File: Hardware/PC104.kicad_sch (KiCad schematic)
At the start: 44 parts, among them J10 J-0532610871, J11 J-TSW-106-05-T-S, J12 J-0532610671, J13 J-0532610471, J14 J-0532610471, J15 J-TSW-106-05-T-S, J16 J-0532610671, J17 J-0532610471, J2 2-Pin Header, J3 ESQ-126-14-G-D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

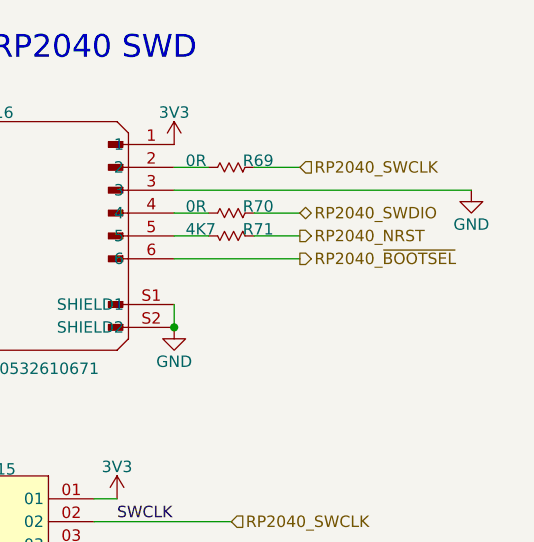
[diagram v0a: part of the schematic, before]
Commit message: Fix RP2040 BOOTSEL
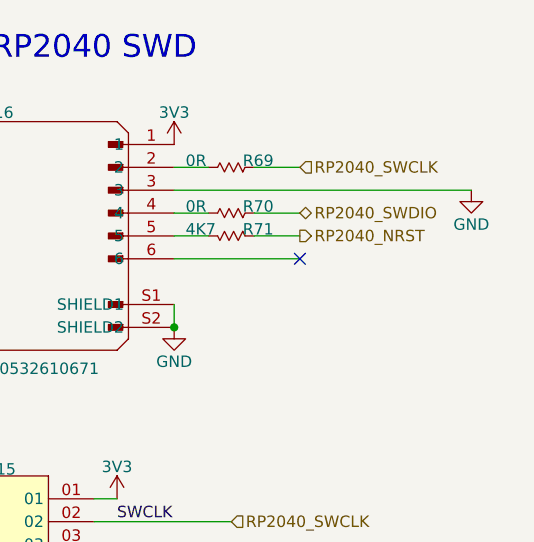
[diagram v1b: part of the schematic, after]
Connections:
- net RP2040_~{BOOTSEL}: no longer J16.6
- no-connect marks 2 -> 3
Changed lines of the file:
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@@
+	)
+	(no_connect
+		(at 356.87 49.53)
 	)
 	(no_connect
@@
 		)
 	)
-	(hierarchical_label "RP2040_~{BOOTSEL}"
-		(shape output)
-		(at 356.87 49.53 0)
-		(effects
-			(font
-				(size 1.27 1.27)
-			)
-			(justify left)
-		)
-	)

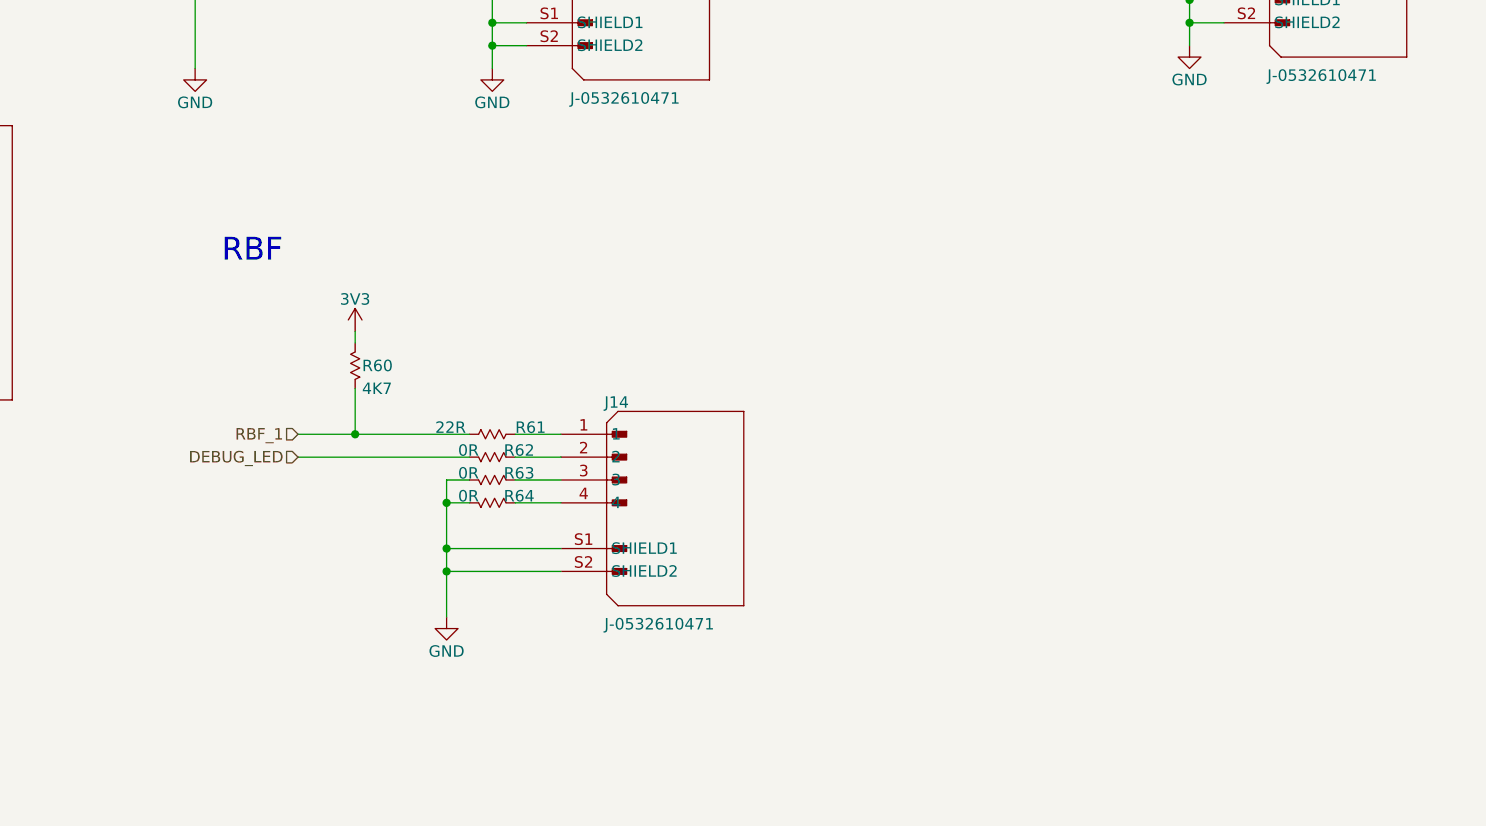
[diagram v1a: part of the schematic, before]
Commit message: Add IOC and second burnwire connector
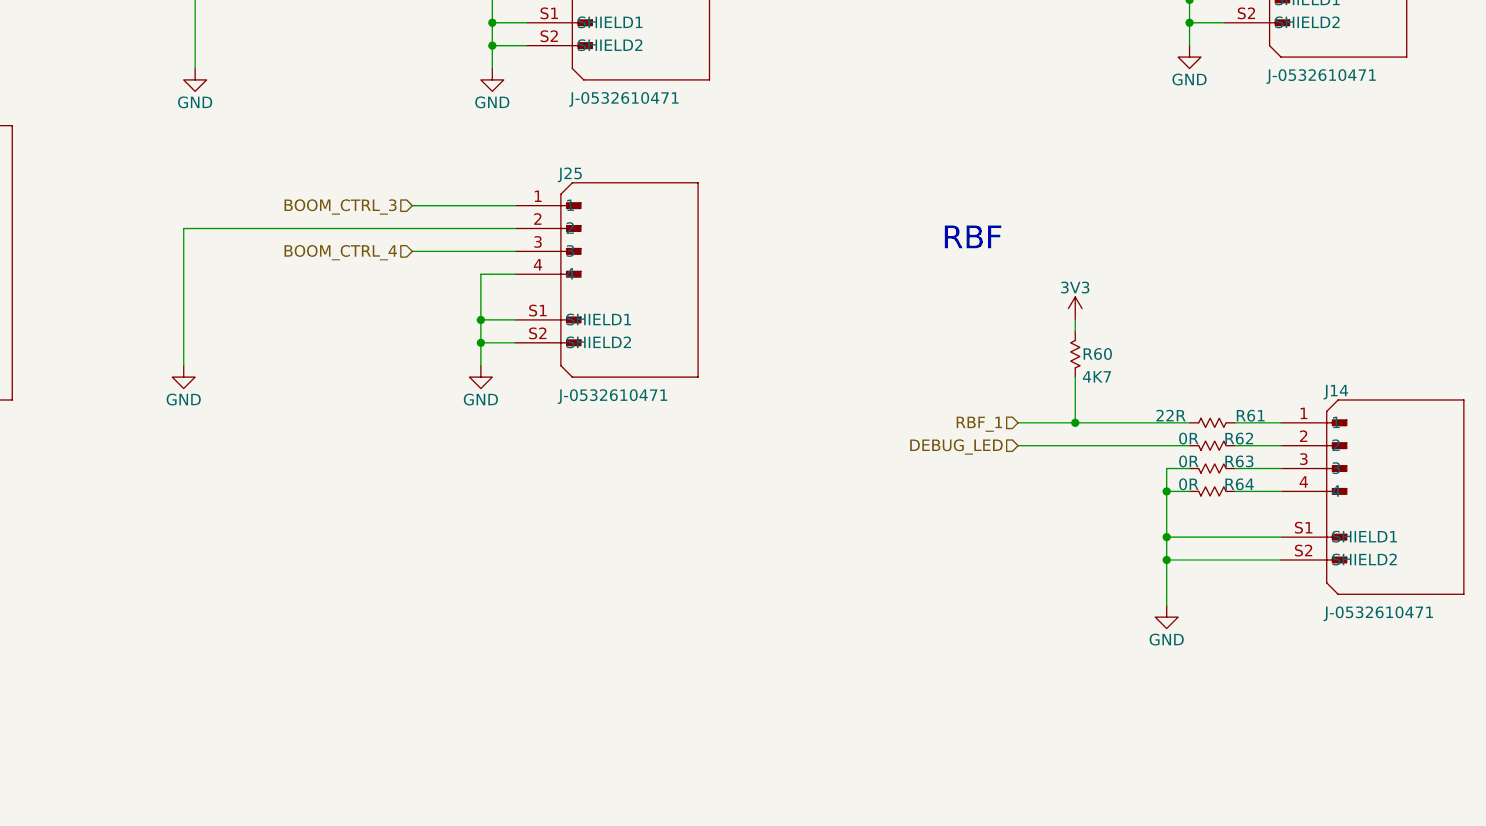
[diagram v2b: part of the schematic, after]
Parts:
- added J25: J-0532610471, J-53261-0471, symbol OBC Development Board:root_0_J-0532610471_OBC Development Board.SchLib
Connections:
- net GND: now also J25.2, J25.4, J25.S1 (SHIELD1), J25.S2 (SHIELD2)
- new net BOOM_CTRL_3: J25.1
- new net BOOM_CTRL_4: J25.3
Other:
- moved on the sheet: J14, R60, R61, R62, R63, R64

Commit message: Assign footprints
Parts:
- C36, C37, C38: footprint (none) -> Capacitor_SMD:C_1206_3216Metric
- D4, D5, D6: footprint (none) -> CTS-SAT-1:D-SML-D12U1WT86
- J10, J9: footprint J-532610871 -> CTS-SAT-1:J-532610871
- J11, J15: footprint J-TSW-106-05-T-S -> CTS-SAT-1:J-TSW-106-05-T-S
- J12, J16, J7: footprint J-0532610671 -> CTS-SAT-1:J-0532610671
- J13, J14, J17, J25, J8: footprint J-53261-0471 -> CTS-SAT-1:J-53261-0471
- J2, J5, J6: footprint (none) -> Connector_PinHeader_1.27mm:PinHeader_1x02_P1.27mm_Vertical
- R50, R51, R52, R53, R54: footprint (none) -> Resistor_SMD:R_0603_1608Metric
- R55, R56, R57, R58, R59, R60, R61, R62, R63, R64, R65, R66, R67, R68, R69, R70, R71: footprint 0603 -> Resistor_SMD:R_0603_1608Metric
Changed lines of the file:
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@@
 			)
 		)
-		(property "Footprint" "0603"
+		(property "Footprint" "Resistor_SMD:R_0603_1608Metric"
 			(at 354.33 187.96 0)
 			(effects
@@
 			)
 		)
-		(property "Footprint" "0603"
+		(property "Footprint" "Resistor_SMD:R_0603_1608Metric"
 			(at 354.33 185.42 0)
 			(effects
@@
 			)
 		)
-		(property "Footprint" "0603"
+		(property "Footprint" "Resistor_SMD:R_0603_1608Metric"
 			(at 285.75 49.53 0)
 			(effects
@@
 			)
 		)
-		(property "Footprint" "J-0532610671"
+		(property "Footprint" "CTS-SAT-1:J-0532610671"
 			(at 264.16 46.99 0)
 			(effects
@@
 			)
 		)
-		(property "Footprint" "J-TSW-106-05-T-S"
+		(property "Footprint" "CTS-SAT-1:J-TSW-106-05-T-S"
 			(at 321.31 83.82 0)
 			(effects
@@
 			)
 		)
-		(property "Footprint" "0603"
+		(property "Footprint" "Resistor_SMD:R_0603_1608Metric"
 			(at 285.75 46.99 0)
 			(effects
@@
 			)
 		)
-		(property "Footprint" "J-53261-0471"
+		(property "Footprint" "CTS-SAT-1:J-53261-0471"
 			(at 377.19 195.58 0)
 			(effects
@@
 			)
 		)
-		(property "Footprint" "0603"
+		(property "Footprint" "Resistor_SMD:R_0603_1608Metric"
 			(at 193.04 157.48 0)
 			(effects
@@
 			)
 		)
-		(property "Footprint" ""
+		(property "Footprint" "Capacitor_SMD:C_1206_3216Metric"
 			(at 108.9152 43.18 0)
 			(effects
@@
 			)
 		)
-		(property "Footprint" ""
+		(property "Footprint" "Resistor_SMD:R_0603_1608Metric"
 			(at 90.424 225.044 90)
 			(effects
@@
 			)
 		)
-		(property "Footprint" "0603"
+		(property "Footprint" "Resistor_SMD:R_0603_1608Metric"
 			(at 351.79 46.99 0)
 			(effects
@@
 			)
 		)
-		(property "Footprint" "J-TSW-106-05-T-S"
+		(property "Footprint" "CTS-SAT-1:J-TSW-106-05-T-S"
 			(at 256.54 83.82 0)
 			(effects
@@
 			)
 		)
-		(property "Footprint" ""
+		(property "Footprint" "CTS-SAT-1:D-SML-D12U1WT86"
 			(at 105.41 241.3 0)
 			(effects
@@
 			)
 		)
-		(property "Footprint" ""
+		(property "Footprint" "Connector_PinHeader_1.27mm:PinHeader_1x02_P1.27mm_Vertical"
 			(at 54.61 167.64 0)
 			(effects
@@
 			)
 		)
-		(property "Footprint" "0603"
+		(property "Footprint" "Resistor_SMD:R_0603_1608Metric"
 			(at 285.75 44.45 0)
 			(effects
@@
 			)
 		)
-		(property "Footprint" "0603"
+		(property "Footprint" "Resistor_SMD:R_0603_1608Metric"
 			(at 351.79 44.45 0)
 			(effects
@@
 			)
 		)
-		(property "Footprint" ""
+		(property "Footprint" "Resistor_SMD:R_0603_1608Metric"
 			(at 90.424 240.284 90)
 			(effects
@@
 			)
 		)
-		(property "Footprint" "J-53261-0471"
+		(property "Footprint" "CTS-SAT-1:J-53261-0471"
 			(at 293.37 138.43 0)
 			(effects
@@
 			)
 		)
-		(property "Footprint" "0603"
+		(property "Footprint" "Resistor_SMD:R_0603_1608Metric"
 			(at 351.79 39.37 0)
 			(effects
@@
 			)
 		)
-		(property "Footprint" ""
+		(property "Footprint" "CTS-SAT-1:D-SML-D12U1WT86"
 			(at 105.41 226.06 0)
 			(effects
@@
 			)
 		)
-		(property "Footprint" ""
+		(property "Footprint" "CTS-SAT-1:D-SML-D12U1WT86"
 			(at 105.41 233.68 0)
 			(effects
@@
 			)
 		)
-		(property "Footprint" ""
+		(property "Footprint" "Resistor_SMD:R_0603_1608Metric"
 			(at 90.424 232.664 90)
 			(effects
@@
 			)
 		)
-		(property "Footprint" "0603"
+		(property "Footprint" "Resistor_SMD:R_0603_1608Metric"
 			(at 354.33 182.88 0)
 			(effects
@@
 			)
 		)
-		(property "Footprint" "0603"
+		(property "Footprint" "Resistor_SMD:R_0603_1608Metric"
 			(at 198.12 167.64 0)
 			(effects
@@
 			)
 		)
-		(property "Footprint" "0603"
+		(property "Footprint" "Resistor_SMD:R_0603_1608Metric"
 			(at 193.04 160.02 0)
 			(effects
@@
 			)
 		)
-		(property "Footprint" ""
+		(property "Footprint" "Connector_PinHeader_1.27mm:PinHeader_1x02_P1.27mm_Vertical"
 			(at 100.33 144.78 0)
 			(effects
@@
 			)
 		)
-		(property "Footprint" "J-53261-0471"
+		(property "Footprint" "CTS-SAT-1:J-53261-0471"
 			(at 370.84 135.89 0)
 			(effects
@@
 			)
 		)
-		(property "Footprint" ""
+		(property "Footprint" "Capacitor_SMD:C_1206_3216Metric"
 			(at 47.9552 242.57 0)
 			(effects
@@
 			)
 		)
-		(property "Footprint" "0603"
+		(property "Footprint" "Resistor_SMD:R_0603_1608Metric"
 			(at 198.12 165.1 0)
 			(effects
@@
 			)
 		)
-		(property "Footprint" "J-532610871"
+		(property "Footprint" "CTS-SAT-1:J-532610871"
 			(at 204.47 109.22 0)
 			(effects
@@
 			)
 		)
-		(property "Footprint" "0603"
+		(property "Footprint" "Resistor_SMD:R_0603_1608Metric"
 			(at 193.04 152.4 0)
 			(effects
@@
 			)
 		)
-		(property "Footprint" "0603"
+		(property "Footprint" "Resistor_SMD:R_0603_1608Metric"
 			(at 341.63 177.8 0)
 			(effects
@@
 			)
 		)
-		(property "Footprint" "0603"
+		(property "Footprint" "Resistor_SMD:R_0603_1608Metric"
 			(at 285.75 39.37 0)
 			(effects
@@
 			)
 		)
-		(property "Footprint" "J-53261-0471"
+		(property "Footprint" "CTS-SAT-1:J-53261-0471"
 			(at 203.2 215.9 0)
 			(effects
@@
 			)
 		)
-		(property "Footprint" "0603"
+		(property "Footprint" "Resistor_SMD:R_0603_1608Metric"
 			(at 354.33 190.5 0)
 			(effects
@@
 			)
 		)
-		(property "Footprint" ""
+		(property "Footprint" "Capacitor_SMD:C_1206_3216Metric"
 			(at 131.7752 62.23 0)
 			(effects
@@
 			)
 		)
-		(property "Footprint" ""
+		(property "Footprint" "Resistor_SMD:R_0603_1608Metric"
 			(at 59.944 260.604 90)
 			(effects
@@
 			)
 		)
-		(property "Footprint" "J-0532610671"
+		(property "Footprint" "CTS-SAT-1:J-0532610671"
 			(at 171.45 63.5 0)
 			(effects
@@
 			)
 		)
-		(property "Footprint" ""
+		(property "Footprint" "Resistor_SMD:R_0603_1608Metric"
 			(at 76.454 260.604 90)
 			(effects
@@
 			)
 		)
-		(property "Footprint" "J-532610871"
+		(property "Footprint" "CTS-SAT-1:J-532610871"
 			(at 215.9 165.1 0)
 			(effects
@@
 			)
 		)
-		(property "Footprint" "J-0532610671"
+		(property "Footprint" "CTS-SAT-1:J-0532610671"
 			(at 330.2 46.99 0)
 			(effects
@@
 			)
 		)
-		(property "Footprint" ""
+		(property "Footprint" "Connector_PinHeader_1.27mm:PinHeader_1x02_P1.27mm_Vertical"
 			(at 101.6 170.18 0)
 			(effects
@@
 			)
 		)
-		(property "Footprint" "J-53261-0471"
+		(property "Footprint" "CTS-SAT-1:J-53261-0471"
 			(at 292.1 171.45 0)
 			(effects

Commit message: Fix diode footprint assignments
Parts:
- D4, D5, D6: footprint CTS-SAT-1:D-SML-D12U1WT86 -> CTS-SAT-2:D-SML-D12U1WT86
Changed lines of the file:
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@@
 			)
 		)
-		(property "Footprint" "CTS-SAT-1:D-SML-D12U1WT86"
+		(property "Footprint" "CTS-SAT-2:D-SML-D12U1WT86"
 			(at 105.41 241.3 0)
 			(effects
@@
 			)
 		)
-		(property "Footprint" "CTS-SAT-1:D-SML-D12U1WT86"
+		(property "Footprint" "CTS-SAT-2:D-SML-D12U1WT86"
 			(at 105.41 226.06 0)
 			(effects
@@
 			)
 		)
-		(property "Footprint" "CTS-SAT-1:D-SML-D12U1WT86"
+		(property "Footprint" "CTS-SAT-2:D-SML-D12U1WT86"
 			(at 105.41 233.68 0)
 			(effects

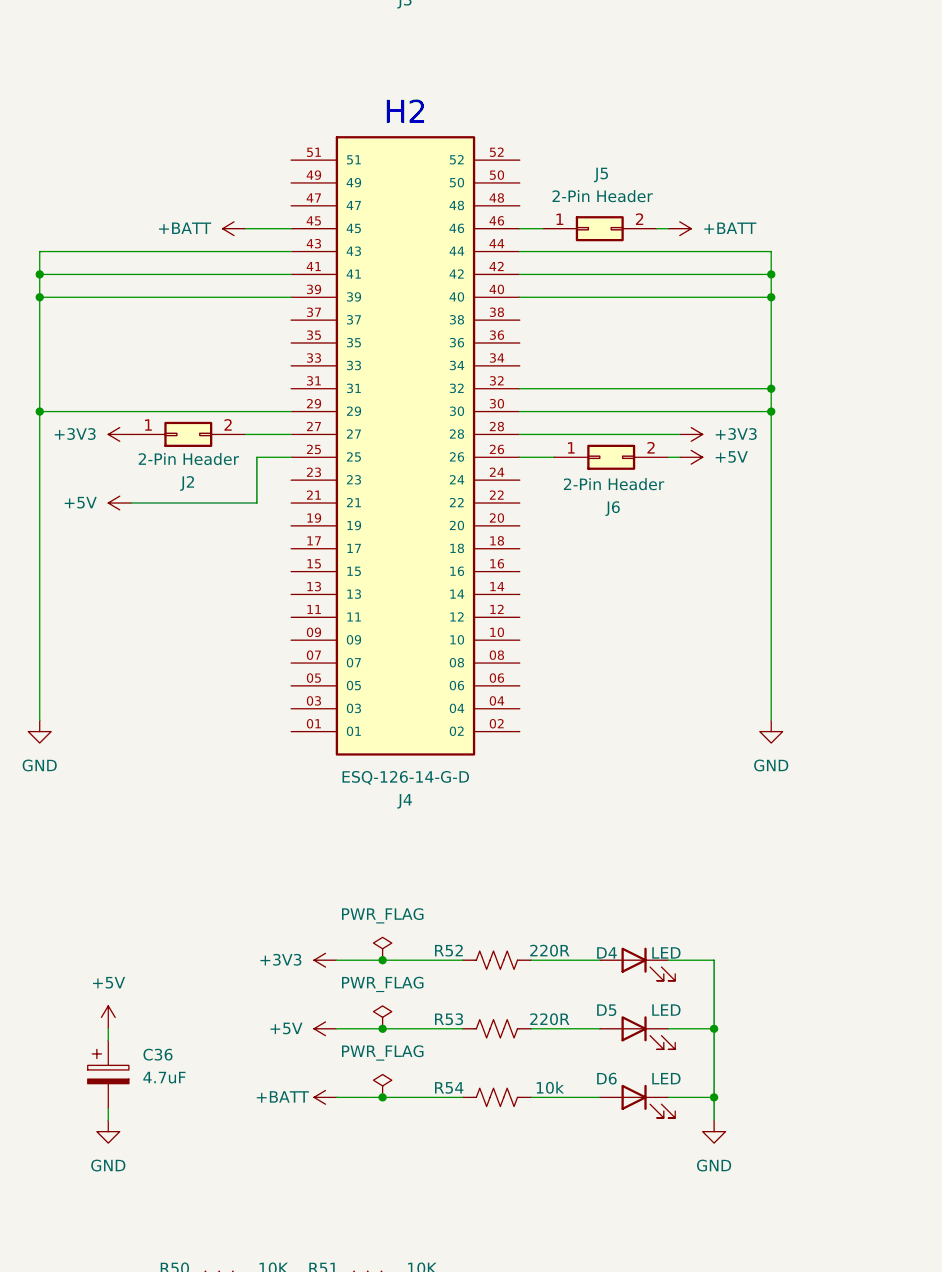
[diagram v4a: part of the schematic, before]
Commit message: H1/2 capacitors and LEDs
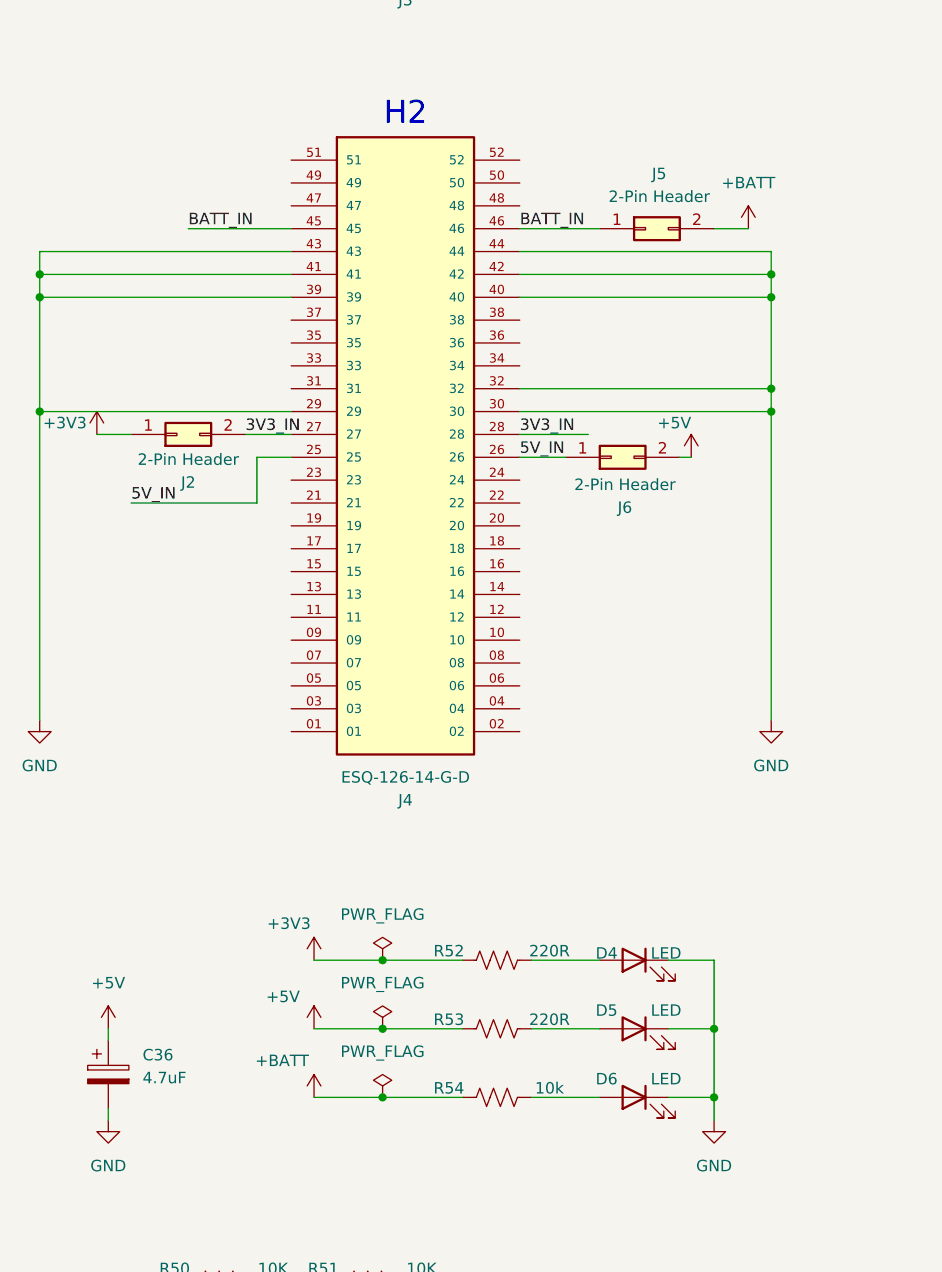
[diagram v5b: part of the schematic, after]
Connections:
- net +3V3: no longer J4.28
- net +5V: no longer J4.25
- net +BATT: no longer J4.45
- net 5V_IN: now reaches J4.26, J6.1 (Pin_1)
- net 5V_IN: now also J4.25
- net 3V3_IN: now reaches J2.2 (Pin_2), J4.27
- net 3V3_IN: now also J4.28
- net BATT_IN: now reaches J4.46, J5.1 (Pin_1)
- net BATT_IN: now also J4.45
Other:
- moved on the sheet: J5, J6

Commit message: STM32 capacitors
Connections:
- net RP2040_NRST: no longer J11.05, R67.1
- net RP2040_SWCLK: no longer J11.02, R65.1
- net RP2040_SWDIO: no longer J11.04, R66.1
- net SWO: now reaches J16.6
- net SWO: now also J15.06
- net RP2040_~{BOOTSEL} renamed STM32_SWO
- net STM32_SWO: no longer J15.06
- new net STM32_NRST: J11.05, R67.1
- new net STM32_SWCLK: J11.02, R65.1
- new net STM32_SWDIO: J11.04, R66.1
- no-connect marks 3 -> 4
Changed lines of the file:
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@@
+	)
+	(no_connect
+		(at 342.9 88.9)
 	)
 	(no_connect
@@
 	(wire
 		(pts
-			(xy 334.01 88.9) (xy 349.25 88.9)
-		)
-		(stroke
-			(width 0)
-			(type default)
-		)
-	)
-	(wire
-		(pts
 			(xy 92.71 63.5) (xy 120.65 63.5)
 		)
@@
 	(wire
 		(pts
+			(xy 334.01 88.9) (xy 342.9 88.9)
+		)
+		(stroke
+			(width 0)
+			(type default)
+		)
+	)
+	(wire
+		(pts
 			(xy 92.71 162.56) (xy 120.65 162.56)
 		)
@@
 			(width 0)
 			(type default)
-		)
-	)
-	(label "NRST"
-		(at 336.55 86.36 0)
-		(effects
-			(font
-				(size 1.27 1.27)
-			)
-			(justify left bottom)
 		)
 	)
@@
 		)
 	)
-	(label "NRST"
-		(at 271.78 86.36 0)
+	(label "SWO"
+		(at 336.55 88.9 0)
 		(effects
 			(font
@@
 		)
 	)
-	(label "SWDIO"
-		(at 271.78 83.82 0)
-		(effects
-			(font
-				(size 1.27 1.27)
-			)
-			(justify left bottom)
-		)
-	)
 	(label "ADCS_UART_TX"
 		(at 52.07 68.58 0)
@@
 	)
 	(label "SWO"
-		(at 336.55 88.9 0)
-		(effects
-			(font
-				(size 1.27 1.27)
-			)
-			(justify left bottom)
-		)
-	)
-	(label "SWCLK"
-		(at 271.78 78.74 0)
-		(effects
-			(font
-				(size 1.27 1.27)
-			)
-			(justify left bottom)
-		)
-	)
-	(label "SWO"
-		(at 271.78 88.9 0)
+		(at 344.17 49.53 0)
 		(effects
 			(font
@@
 		)
 	)
-	(label "SWCLK"
-		(at 336.55 78.74 0)
-		(effects
-			(font
-				(size 1.27 1.27)
-			)
-			(justify left bottom)
-		)
-	)
 	(label "BATT_IN"
 		(at 55.88 144.78 0)
@@
 	(label "3V3_IN"
 		(at 92.71 167.64 0)
-		(effects
-			(font
-				(size 1.27 1.27)
-			)
-			(justify left bottom)
-		)
-	)
-	(label "SWDIO"
-		(at 336.55 83.82 0)
 		(effects
 			(font
@@
 		(effects
 			(font
-				(size 1.27 1.27)
-			)
-			(justify left)
-		)
-	)
-	(hierarchical_label "RP2040_~{BOOTSEL}"
-		(shape output)
-		(at 349.25 88.9 0)
-		(effects
-			(font
